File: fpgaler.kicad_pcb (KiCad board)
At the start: 4 copper layers, 245.2 x 139.3 mm, 252 parts, among them J1 USB_C_Receptacle_USB2.0, J2 BATT, J3 JTAG, J4 FTDI_RST, J5 VGA, J6 DB9 Expander, Q1 BC817, SW1 RotaryEncoder_Switch, SW2 RotaryEncoder_Switch, SW3 K1, SW4 K2, SW5 PROGRAMN, SW6 K3, SW7 FPGA GSRN, SW8 K4, U1 TLV62569DRL, U10 XC6206PxxxMR, U11 IS62WV51216BLL-55TLI, U2 TLV62569DRL, U3 NCP115-2.5, U4 BQ24232, U5 93LC56BT-I/OT, U6 FT2232HL, U7 CAT24C128, U8 LFE5U-25F-8MG285C, U9 W25Q128JVP, X1 27MHz, Y1 7M-12.000MAAJ

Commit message: Routing sram
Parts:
- added R126: 22R, Resistor_SMD:R_0402_1005Metric_Pad0.72x0.64mm_HandSolder, F.Cu at (212.6, 117.6)
- added R127: 22R, Resistor_SMD:R_0402_1005Metric_Pad0.72x0.64mm_HandSolder, F.Cu at (208.9, 117.9)
- added R128: 22R, Resistor_SMD:R_0402_1005Metric_Pad0.72x0.64mm_HandSolder, F.Cu at (212.6, 116.6)
- added R129: 22R, Resistor_SMD:R_0402_1005Metric_Pad0.72x0.64mm_HandSolder, F.Cu at (212.6, 115.6)
- added R130: 22R, Resistor_SMD:R_0402_1005Metric_Pad0.72x0.64mm_HandSolder, F.Cu at (212.6, 101.4)
- added R131: 22R, Resistor_SMD:R_0402_1005Metric_Pad0.72x0.64mm_HandSolder, F.Cu at (212.6, 100.4)
- added R132: 22R, Resistor_SMD:R_0402_1005Metric_Pad0.72x0.64mm_HandSolder, F.Cu at (212.6, 102.4)
- added R133: 22R, Resistor_SMD:R_0402_1005Metric_Pad0.72x0.64mm_HandSolder, F.Cu at (212.6, 105.4)
- added R134: 22R, Resistor_SMD:R_0402_1005Metric_Pad0.72x0.64mm_HandSolder, F.Cu at (212.6, 104.4)
- added R135: 22R, Resistor_SMD:R_0402_1005Metric_Pad0.72x0.64mm_HandSolder, F.Cu at (212.6, 103.4)
- added R136: 22R, Resistor_SMD:R_0402_1005Metric_Pad0.72x0.64mm_HandSolder, F.Cu at (208.9, 106.9)
- added R137: 22R, Resistor_SMD:R_0402_1005Metric_Pad0.72x0.64mm_HandSolder, F.Cu at (208.9, 108.9)
- added R138: 22R, Resistor_SMD:R_0402_1005Metric_Pad0.72x0.64mm_HandSolder, F.Cu at (212.6, 106.4)
- added R139: 22R, Resistor_SMD:R_0402_1005Metric_Pad0.72x0.64mm_HandSolder, F.Cu at (212.6, 107.4)
- added R140: 22R, Resistor_SMD:R_0402_1005Metric_Pad0.72x0.64mm_HandSolder, F.Cu at (208.9, 107.9)
- added R141: 22R, Resistor_SMD:R_0402_1005Metric_Pad0.72x0.64mm_HandSolder, F.Cu at (208.9, 110.9)
- added R142: 22R, Resistor_SMD:R_0402_1005Metric_Pad0.72x0.64mm_HandSolder, F.Cu at (208.9, 109.9)
- added R143: 22R, Resistor_SMD:R_0402_1005Metric_Pad0.72x0.64mm_HandSolder, F.Cu at (208.9, 111.9)
- added R144: 22R, Resistor_SMD:R_0402_1005Metric_Pad0.72x0.64mm_HandSolder, F.Cu at (212.6, 109.4)
- added R145: 22R, Resistor_SMD:R_0402_1005Metric_Pad0.72x0.64mm_HandSolder, F.Cu at (212.6, 108.4)
- added R146: 22R, Resistor_SMD:R_0402_1005Metric_Pad0.72x0.64mm_HandSolder, F.Cu at (212.6, 110.5)
- added R147: 22R, Resistor_SMD:R_0402_1005Metric_Pad0.72x0.64mm_HandSolder, F.Cu at (212.6, 112.6)
- added R148: 22R, Resistor_SMD:R_0402_1005Metric_Pad0.72x0.64mm_HandSolder, F.Cu at (208.9, 113.9)
- added R149: 22R, Resistor_SMD:R_0402_1005Metric_Pad0.72x0.64mm_HandSolder, F.Cu at (208.9, 112.9)
- added R150: 22R, Resistor_SMD:R_0402_1005Metric_Pad0.72x0.64mm_HandSolder, F.Cu at (212.6, 111.6)
- added R151: 22R, Resistor_SMD:R_0402_1005Metric_Pad0.72x0.64mm_HandSolder, F.Cu at (212.6, 113.6)
- added R152: 22R, Resistor_SMD:R_0402_1005Metric_Pad0.72x0.64mm_HandSolder, F.Cu at (208.9, 115.9)
- added R153: 22R, Resistor_SMD:R_0402_1005Metric_Pad0.72x0.64mm_HandSolder, F.Cu at (208.9, 114.9)
- added R154: 22R, Resistor_SMD:R_0402_1005Metric_Pad0.72x0.64mm_HandSolder, F.Cu at (208.9, 116.9)
- added R155: 22R, Resistor_SMD:R_0402_1005Metric_Pad0.72x0.64mm_HandSolder, F.Cu at (212.6, 114.6)
- added R156: 22R, Resistor_SMD:R_0402_1005Metric_Pad0.72x0.64mm_HandSolder, F.Cu at (208.9, 102.9)
- added R157: 22R, Resistor_SMD:R_0402_1005Metric_Pad0.72x0.64mm_HandSolder, F.Cu at (208.9, 104.9)
- added R158: 22R, Resistor_SMD:R_0402_1005Metric_Pad0.72x0.64mm_HandSolder, F.Cu at (208.9, 105.9)
- added R159: 22R, Resistor_SMD:R_0402_1005Metric_Pad0.72x0.64mm_HandSolder, F.Cu at (208.9, 101.9)
- added R160: 22R, Resistor_SMD:R_0402_1005Metric_Pad0.72x0.64mm_HandSolder, F.Cu at (208.9, 98.9)
- added R161: 22R, Resistor_SMD:R_0402_1005Metric_Pad0.72x0.64mm_HandSolder, F.Cu at (208.9, 103.9)
- added R162: 22R, Resistor_SMD:R_0402_1005Metric_Pad0.72x0.64mm_HandSolder, F.Cu at (208.9, 99.9)
- added R163: 22R, Resistor_SMD:R_0402_1005Metric_Pad0.72x0.64mm_HandSolder, F.Cu at (208.9, 100.9)
- added R164: 22R, Resistor_SMD:R_0402_1005Metric_Pad0.72x0.64mm_HandSolder, F.Cu at (212.6, 98.4)
- added R165: 22R, Resistor_SMD:R_0402_1005Metric_Pad0.72x0.64mm_HandSolder, F.Cu at (212.6, 99.4)
- R10, R114, R115, R116, R117, R118, R119, R120, R121, R122, R123, R124, R125, R52, R53, R54, R55, R56, R57, R59, R60, R61, R67, R68, R69, R70, R73, R74, R75, R76, R77, R78, R79, R80, R81, R82, R83, R84, R85, R86, R87, R88, R89, R9, R90: footprint Resistor_SMD:R_0603_1608Metric -> Resistor_SMD:R_0402_1005Metric_Pad0.72x0.64mm_HandSolder
- moved C57 34.7 mm to (250.6, 93.5)
- moved C58 34.7 mm to (250.8, 110.3)
- moved TP58 27.5 mm to (237.2, 127.0)
- moved TP59 27.5 mm to (239.7, 125.7)
- moved TP60 27.5 mm to (239.7, 128.2)
- moved TP62 27.5 mm to (239.7, 130.8)
- moved TP64 27.5 mm to (234.6, 130.8)
- moved TP61 27.5 mm to (242.2, 129.5)
- moved TP63 27.5 mm to (237.2, 129.5)
- moved U11 8.55 mm to (225.1, 107.7)
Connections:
- U8 pad A16: unconnected-(U8F-PL20B-PadA16) -> Net-(U8F-PL20B)
- U8 pad A17: /FPGA/A5 -> Net-(U8F-PL23A/PCLKT7_1)
- U8 pad A2: unconnected-(U8C-PR20C/GR_PCLK2_0-PadA2) -> /FPGA/VGA_B0
- U8 pad A3: unconnected-(U8C-PR20A/GR_PCLK2_1-PadA3) -> /FPGA/VGA_G1
- U8 pad B1: unconnected-(U8C-PR23B/PCLKC2_1-PadB1) -> /FPGA/VGA_B2
- U8 pad B15: /FPGA/A7 -> Net-(U8F-PL20A/GR_PCLK7_1)
- U8 pad B17: /FPGA/A6 -> Net-(U8F-PL23B/PCLKC7_1)
- U8 pad B18: /FPGA/A12 -> Net-(U8F-PL23C/PCLKT7_0)
- U8 pad B2: unconnected-(U8C-PR20B-PadB2) -> /FPGA/VGA_G2
- U8 pad B4: unconnected-(U8C-PR14C/VREF1_2-PadB4) -> /FPGA/VGA_R0
- U8 pad C1: unconnected-(U8C-PR23C/PCLKT2_0-PadC1) -> /FPGA/VGA_HSYNC
- U8 pad C15: /FPGA/~{OE} -> Net-(U8F-PL14C/VREF1_7)
- U8 pad C16: /FPGA/~{UB} -> Net-(U8F-PL20C/GR_PCLK7_0)
- U8 pad C17: /FPGA/A13 -> Net-(U8F-PL23D/PCLKC7_0)
- U8 pad C18: /FPGA/A14 -> Net-(U8E-PL26B/PCLKC6_1)
- U8 pad C2: unconnected-(U8C-PR17B-PadC2) -> /FPGA/VGA_G0
- U8 pad C3: unconnected-(U8C-PR14D-PadC3) -> /FPGA/VGA_R1
- U8 pad D1: unconnected-(U8C-PR23D/PCLKC2_0-PadD1) -> /FPGA/VGA_VSYNC
- U8 pad D15: /FPGA/~{LB} -> Net-(U8F-PL17A)
- U8 pad D16: /FPGA/IO15 -> Net-(U8F-PL17B)
- U8 pad D17: /FPGA/A15 -> Net-(U8E-PL26A/PCLKT6_1)
- U8 pad D18: /FPGA/A16 -> Net-(U8E-PL26C/PCLKT6_0)
- U8 pad D2: unconnected-(U8C-PR23A/PCLKT2_1-PadD2) -> /FPGA/VGA_B1
- U8 pad D3: unconnected-(U8C-PR17A-PadD3) -> /FPGA/VGA_R2
- U8 pad F15: /FPGA/IO14 -> Net-(U8E-PL29C/GR_PCLK6_1)
- U8 pad F16: /FPGA/~{WE} -> Net-(U8E-PL29B)
- U8 pad F17: /FPGA/IO07 -> Net-(U8E-PL29A/GR_PCLK6_0)
- U8 pad F18: /FPGA/IO06 -> Net-(U8E-PL26D/PCLKC6_0)
- U8 pad G15: /FPGA/IO13 -> Net-(U8E-PL35A)
- U8 pad G16: /FPGA/IO12 -> Net-(U8E-PL29D)
- U8 pad G18: /FPGA/IO05 -> Net-(U8E-PL32A)
- U8 pad H15: /FPGA/IO10 -> Net-(U8E-PL35B/VREF1_6)
- U8 pad H16: /FPGA/IO11 -> Net-(U8E-PL35C)
- U8 pad H17: /FPGA/IO04 -> Net-(U8E-PL32B)
- U8 pad H18: /FPGA/IO03 -> Net-(U8E-PL38D)
- U8 pad J16: /FPGA/IO09 -> Net-(U8E-PL35D)
- U8 pad J17: /FPGA/IO02 -> Net-(U8E-PL38C)
- U8 pad J18: /FPGA/IO01 -> Net-(U8E-PL41A)
- U8 pad K15: /FPGA/IO08 -> Net-(U8E-PL41D)
- U8 pad K16: /FPGA/A18 -> Net-(U8E-PL41C)
- U8 pad K17: /FPGA/IO00 -> Net-(U8E-PL44A)
- U8 pad K18: /FPGA/~{CS1} -> Net-(U8E-PL41B)
- U8 pad L15: /FPGA/A9 -> Net-(U8E-PL44C)
- U8 pad L16: /FPGA/A8 -> Net-(U8E-PL44D)
- U8 pad L18: /FPGA/A0 -> Net-(U8E-PL44B)
- U8 pad M16: /FPGA/A10 -> Net-(U8E-PL47C/LLC_GPLL0T_IN)
- U8 pad M17: /FPGA/A1 -> Net-(U8E-PL47D/LLC_GPLL0C_IN)
- U8 pad M18: /FPGA/A2 -> Net-(U8G-PB6B/D4/MOSI2/IO4)
- U8 pad N15: /FPGA/A4 -> Net-(U8G-PB4A/D7/IO7)
- U8 pad N16: /FPGA/A11 -> Net-(U8G-PB4B/D6/IO6)
- U8 pad N17: /FPGA/A3 -> Net-(U8G-PB6A/D5/MISO2/IO5)
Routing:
- net Net-(U8G-PB4A/D7/IO7): track 0.00 -> 15.2 mm, vias 0 -> 2
- net Net-(U8G-PB6A/D5/MISO2/IO5): track 0.00 -> 13.8 mm
- net Net-(U8E-PL26A/PCLKT6_1): track 0.00 -> 13.2 mm
- net Net-(U8E-PL29B): track 0.00 -> 12.8 mm
- net Net-(U8F-PL23C/PCLKT7_0): track 0.00 -> 12.8 mm
- net Net-(U8F-PL23D/PCLKC7_0): track 0.00 -> 12.7 mm
- net Net-(U8G-PB6B/D4/MOSI2/IO4): track 0.00 -> 12.3 mm
- net Net-(U8E-PL26C/PCLKT6_0): track 0.00 -> 12.2 mm
- net Net-(U8E-PL47D/LLC_GPLL0C_IN): track 0.00 -> 12.2 mm
- net Net-(U8E-PL29A/GR_PCLK6_0): track 0.00 -> 11.5 mm
- net Net-(U8E-PL26B/PCLKC6_1): track 0.00 -> 11.2 mm
- net /FPGA/A14: track 25.0 -> 35.5 mm, vias 0 -> 1
- net Net-(U8G-PB4B/D6/IO6): track 0.00 -> 10.5 mm, vias 0 -> 2
- net Net-(U8E-PL44B): track 0.00 -> 10.4 mm
- net Net-(U8E-PL47C/LLC_GPLL0T_IN): track 0.00 -> 10.3 mm, vias 0 -> 2
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
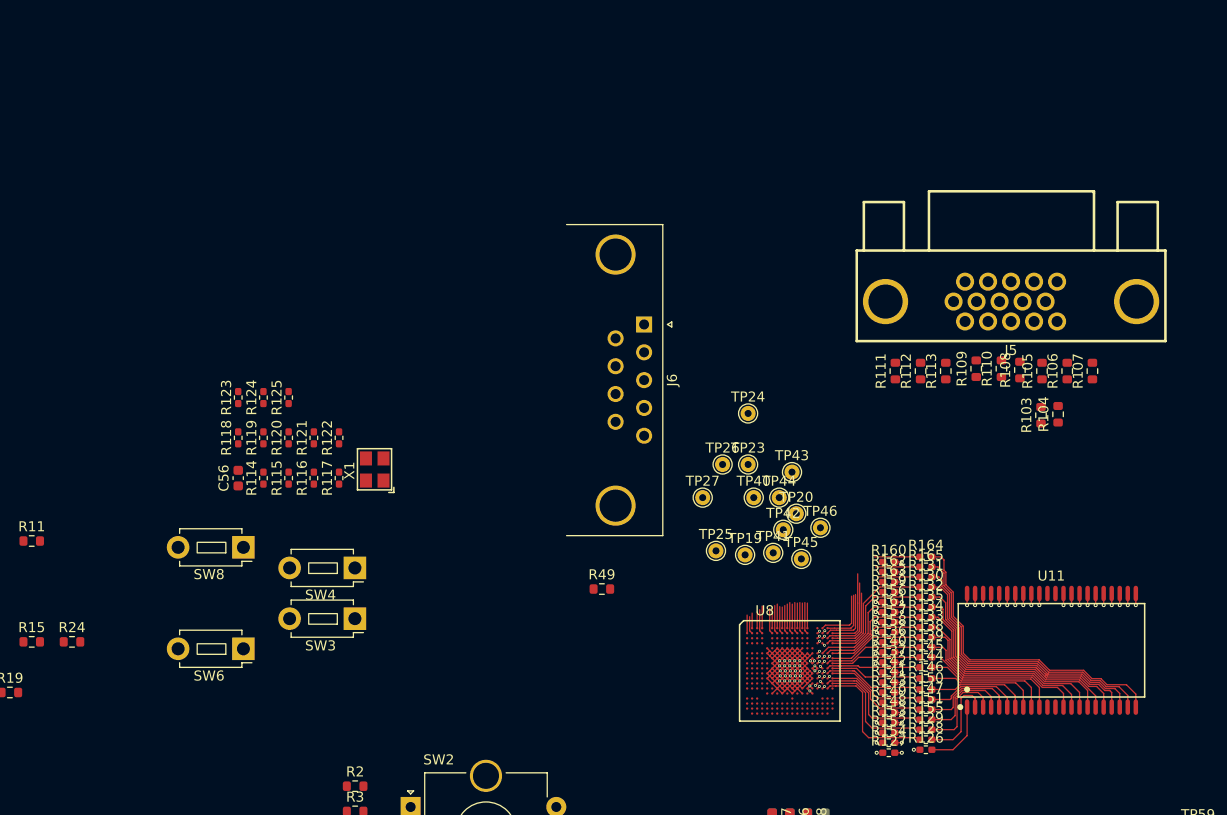
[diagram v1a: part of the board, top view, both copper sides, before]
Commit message: Complete SRAM, and routing VGA
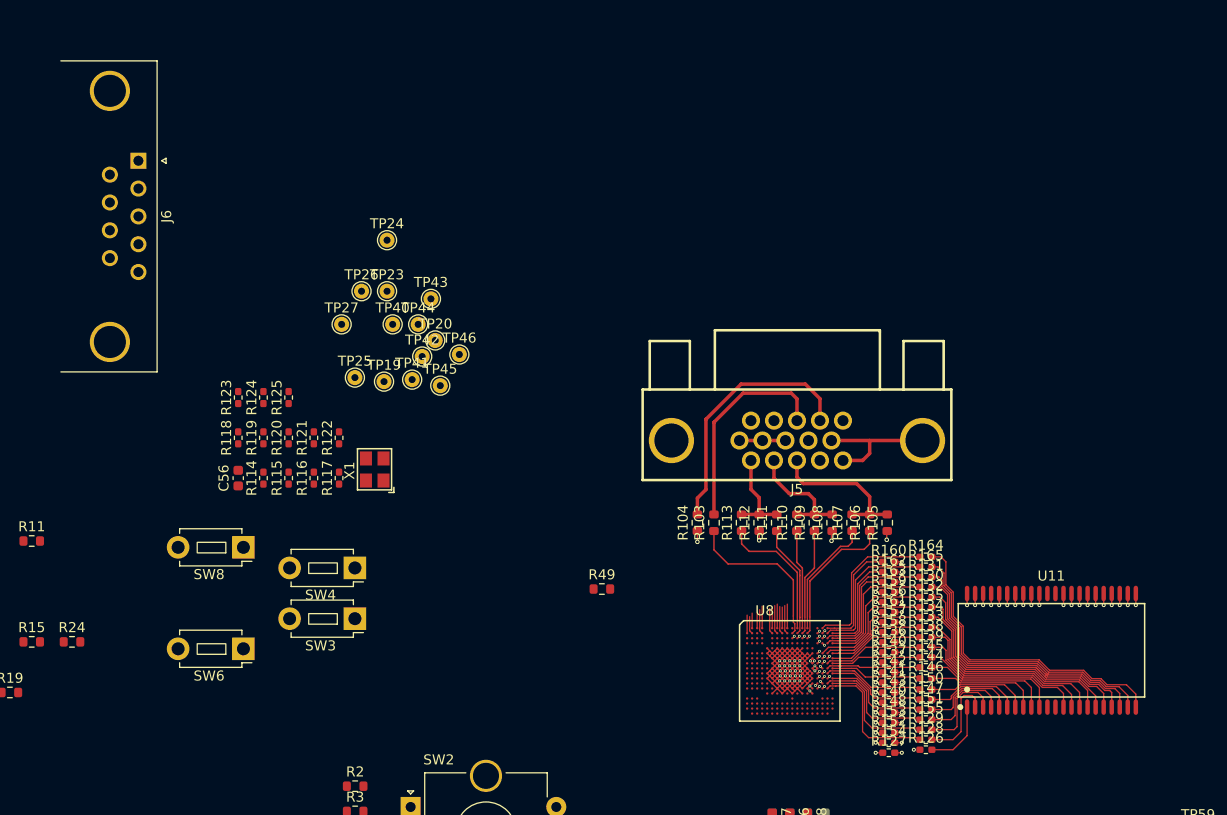
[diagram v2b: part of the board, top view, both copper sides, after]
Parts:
- moved J6 52.9 mm to (134.2, 59.0)
- moved TP23 39.9 mm to (158.9, 72.0)
- moved TP24 39.9 mm to (158.9, 66.9)
- moved TP26 39.9 mm to (156.4, 72.0)
- moved TP40 39.9 mm to (159.5, 75.2)
- moved TP41 39.9 mm to (161.4, 80.8)
- moved TP42 39.9 mm to (162.4, 78.5)
- moved TP43 39.9 mm to (163.3, 72.7)
- moved TP19 39.9 mm to (158.7, 81.0)
- moved TP20 39.9 mm to (163.8, 76.8)
- moved TP25 39.9 mm to (155.8, 80.5)
- moved TP27 39.9 mm to (154.4, 75.2)
- moved TP44 39.9 mm to (162.1, 75.2)
- moved TP45 39.9 mm to (164.2, 81.3)
- moved TP46 39.9 mm to (166.2, 78.2)
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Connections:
- R114 pad 2: Net-(U8A-PT29A/PCLKT0_0) -> Net-(U8B-PT33A/PCLKT1_1)
- R115 pad 2: Net-(U8A-PT29B/PCLKC0_0) -> Net-(U8B-PT33B/PCLKC1_1)
- R131 pad 1: Net-(U8E-PL26B/PCLKC6_1) -> Net-(U8F-PL23D/PCLKC7_0)
- R131 pad 2: /FPGA/A17 -> /FPGA/A14
- R160 pad 1: Net-(U8F-PL20B) -> Net-(U8F-PL23A/PCLKT7_1)
- R160 pad 2: /FPGA/A5 -> /FPGA/A17
- R162 pad 1: Net-(U8F-PL23A/PCLKT7_1) -> Net-(U8F-PL23C/PCLKT7_0)
- R162 pad 2: /FPGA/A6 -> unconnected-(R162-Pad2)
- R163 pad 1: Net-(U8F-PL23B/PCLKC7_1) -> Net-(U8E-PL26B/PCLKC6_1)
- R163 pad 2: /FPGA/A14 -> /FPGA/A6
- R164 pad 1: Net-(U8F-PL23C/PCLKT7_0) -> Net-(U8F-PL20B)
- R165 pad 1: Net-(U8F-PL23D/PCLKC7_0) -> Net-(U8F-PL23B/PCLKC7_1)
- TP19 pad 1: Net-(U8A-PT27A/PCLKT0_1) -> unconnected-(TP19-Pad1)
- TP20 pad 1: Net-(U8A-PT27B/PCLKC0_1) -> unconnected-(TP20-Pad1)
- TP23 pad 1: Net-(U8B-PT33A/PCLKT1_1) -> unconnected-(TP23-Pad1)
- TP24 pad 1: Net-(U8B-PT33B/PCLKC1_1) -> unconnected-(TP24-Pad1)
- TP40 pad 1: Net-(U8F-PL2A) -> unconnected-(TP40-Pad1)
- TP41 pad 1: Net-(U8F-PL2B) -> unconnected-(TP41-Pad1)
- TP42 pad 1: Net-(U8F-PL5A) -> unconnected-(TP42-Pad1)
- TP43 pad 1: Net-(U8F-PL8A) -> unconnected-(TP43-Pad1)
- TP44 pad 1: Net-(U8F-PL8B) -> unconnected-(TP44-Pad1)
- TP45 pad 1: Net-(U8F-PL14A) -> unconnected-(TP45-Pad1)
- TP46 pad 1: Net-(U8F-PL14B) -> unconnected-(TP46-Pad1)
- U8 pad A10: Net-(U8A-PT27B/PCLKC0_1) -> unconnected-(U8A-PT27B/PCLKC0_1-PadA10)
- U8 pad A11: Net-(U8A-PT27A/PCLKT0_1) -> /FPGA/VGA_R2
- U8 pad A12: Net-(U8F-PL5A) -> /FPGA/VGA_G2
- U8 pad A13: Net-(U8F-PL14B) -> /FPGA/VGA_B2
- U8 pad A2: /FPGA/VGA_B0 -> unconnected-(U8C-PR20C/GR_PCLK2_0-PadA2)
- U8 pad A3: /FPGA/VGA_G1 -> unconnected-(U8C-PR20A/GR_PCLK2_1-PadA3)
- U8 pad B1: /FPGA/VGA_B2 -> unconnected-(U8C-PR23B/PCLKC2_1-PadB1)
- U8 pad B10: Net-(U8A-PT29A/PCLKT0_0) -> /FPGA/VGA_HSYNC
- U8 pad B11: /FPGA/sda -> /FPGA/VGA_R0
- U8 pad B12: Net-(U8F-PL2B) -> /FPGA/VGA_G1
- U8 pad B13: Net-(U8F-PL14A) -> /FPGA/VGA_B1
- U8 pad B2: /FPGA/VGA_G2 -> unconnected-(U8C-PR20B-PadB2)
- U8 pad B4: /FPGA/VGA_R0 -> unconnected-(U8C-PR14C/VREF1_2-PadB4)
- U8 pad C1: /FPGA/VGA_HSYNC -> unconnected-(U8C-PR23C/PCLKT2_0-PadC1)
- U8 pad C10: Net-(U8A-PT29B/PCLKC0_0) -> /FPGA/VGA_VSYNC
- U8 pad C11: /FPGA/scl -> /FPGA/VGA_R1
- U8 pad C12: Net-(U8F-PL2A) -> /FPGA/VGA_G0
- U8 pad C13: Net-(U8F-PL8B) -> /FPGA/VGA_B0
- U8 pad C2: /FPGA/VGA_G0 -> unconnected-(U8C-PR17B-PadC2)
- U8 pad C3: /FPGA/VGA_R1 -> unconnected-(U8C-PR14D-PadC3)
- U8 pad D1: /FPGA/VGA_VSYNC -> unconnected-(U8C-PR23D/PCLKC2_0-PadD1)
- U8 pad D13: Net-(U8F-PL8A) -> unconnected-(U8F-PL8A-PadD13)
- U8 pad D2: /FPGA/VGA_B1 -> unconnected-(U8C-PR23A/PCLKT2_1-PadD2)
- U8 pad D3: /FPGA/VGA_R2 -> unconnected-(U8C-PR17A-PadD3)
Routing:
- net GND: track 98.7 -> 128.0 mm
- net /FPGA/A17: track 0.70 -> 26.5 mm, vias 1 -> 2
- net /VSYNC: track 0.00 -> 25.4 mm
- net /HSYNC: track 0.00 -> 21.0 mm
- net /FPGA/VGA_VSYNC: track 0.00 -> 18.6 mm, vias 0 -> 2
- net /FPGA/VGA_HSYNC: track 0.00 -> 16.5 mm
- net /B: track 0.00 -> 15.0 mm
- net /FPGA/VGA_B0: track 1.50 -> 15.8 mm, vias 0 -> 2
- net /FPGA/VGA_B1: track 0.00 -> 14.1 mm
- net /FPGA/VGA_R1: track 0.00 -> 13.8 mm, vias 0 -> 2
- net /FPGA/VGA_R2: track 0.00 -> 13.6 mm
- net /FPGA/VGA_G0: track 0.00 -> 11.9 mm, vias 0 -> 2
- net /G: track 0.00 -> 11.7 mm
- net /FPGA/VGA_B2: track 1.80 -> 12.0 mm
- net Net-(U8F-PL20B): track 5.80 -> 15.6 mm
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
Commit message: Place db9, encoder, btn and leds. Continue routing.
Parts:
- removed R49: 0R, Resistor_SMD:R_0603_1608Metric
- added J7: DB9 Expander, Connector_Dsub:DSUB-9_Pins_Horizontal_P2.77x2.84mm_EdgePinOffset4.94mm_Housed_MountingHolesOffset4.94mm, F.Cu at (90.6, 117.1)
- added R166: 22R, Resistor_SMD:R_0402_1005Metric_Pad0.72x0.64mm_HandSolder, F.Cu at (107.3, 41.9)
- added TP10: TestPoint, TestPoint:TestPoint_THTPad_D1.5mm_Drill0.7mm, F.Cu at (105.0, 115.9)
- added TP11: TestPoint, TestPoint:TestPoint_THTPad_D1.5mm_Drill0.7mm, F.Cu at (104.6, 43.4)
- added TP12: TestPoint, TestPoint:TestPoint_THTPad_D1.5mm_Drill0.7mm, F.Cu at (102.0, 42.1)
- added TP13: TestPoint, TestPoint:TestPoint_THTPad_D1.5mm_Drill0.7mm, F.Cu at (104.6, 40.8)
- added TP14: TestPoint, TestPoint:TestPoint_THTPad_D1.5mm_Drill0.7mm, F.Cu at (102.0, 39.6)
- added TP15: TestPoint, TestPoint:TestPoint_THTPad_D1.5mm_Drill0.7mm, F.Cu at (104.6, 38.3)
- added TP16: TestPoint, TestPoint:TestPoint_THTPad_D1.5mm_Drill0.7mm, F.Cu at (102.0, 37.0)
- added TP17: TestPoint, TestPoint:TestPoint_THTPad_D1.5mm_Drill0.7mm, F.Cu at (104.6, 35.8)
- added TP18: TestPoint, TestPoint:TestPoint_THTPad_D1.5mm_Drill0.7mm, F.Cu at (102.0, 34.5)
- added TP2: TestPoint, TestPoint:TestPoint_THTPad_D1.5mm_Drill0.7mm, F.Cu at (105.0, 126.1)
- added TP21: TestPoint, TestPoint:TestPoint_THTPad_D1.5mm_Drill0.7mm, F.Cu at (104.6, 33.2)
- added TP22: TestPoint, TestPoint:TestPoint_THTPad_D1.5mm_Drill0.7mm, F.Cu at (99.0, 86.0)
- added TP28: TestPoint, TestPoint:TestPoint_THTPad_D1.5mm_Drill0.7mm, F.Cu at (96.5, 84.0)
- added TP29: TestPoint, TestPoint:TestPoint_THTPad_D1.5mm_Drill0.7mm, F.Cu at (99.0, 82.0)
- added TP3: TestPoint, TestPoint:TestPoint_THTPad_D1.5mm_Drill0.7mm, F.Cu at (102.5, 124.8)
- added TP30: TestPoint, TestPoint:TestPoint_THTPad_D1.5mm_Drill0.7mm, F.Cu at (96.5, 80.0)
- added TP31: TestPoint, TestPoint:TestPoint_THTPad_D1.5mm_Drill0.7mm, F.Cu at (99.0, 78.0)
- added TP32: TestPoint, TestPoint:TestPoint_THTPad_D1.5mm_Drill0.7mm, F.Cu at (96.5, 76.0)
- added TP33: TestPoint, TestPoint:TestPoint_THTPad_D1.5mm_Drill0.7mm, F.Cu at (99.0, 74.0)
- added TP34: TestPoint, TestPoint:TestPoint_THTPad_D1.5mm_Drill0.7mm, F.Cu at (96.5, 72.0)
- added TP4: TestPoint, TestPoint:TestPoint_THTPad_D1.5mm_Drill0.7mm, F.Cu at (105.0, 123.5)
- added TP5: TestPoint, TestPoint:TestPoint_THTPad_D1.5mm_Drill0.7mm, F.Cu at (102.5, 122.3)
- added TP6: TestPoint, TestPoint:TestPoint_THTPad_D1.5mm_Drill0.7mm, F.Cu at (105.0, 121.0)
- added TP7: TestPoint, TestPoint:TestPoint_THTPad_D1.5mm_Drill0.7mm, F.Cu at (102.5, 119.7)
- added TP8: TestPoint, TestPoint:TestPoint_THTPad_D1.5mm_Drill0.7mm, F.Cu at (105.0, 118.5)
- added TP9: TestPoint, TestPoint:TestPoint_THTPad_D1.5mm_Drill0.7mm, F.Cu at (102.5, 117.2)
- R91, R92, R93, R94: moved to F.Cu
- moved R17 134.4 mm to (126.2, 95.0), turned to 90 degrees
- moved C7 132.0 mm to (128.8, 90.0), turned to 90 degrees
- moved C5 128.6 mm to (126.3, 89.8), turned to 90 degrees
- moved R22 125.8 mm to (129.6, 95.1), turned to 90 degrees
- moved TP27 123.9 mm to (268.5, 123.6), turned to 180 degrees
- moved TP24 123.6 mm to (264.0, 132.0), turned to 180 degrees
- moved TP26 123.1 mm to (266.5, 126.9), turned to 180 degrees
- moved TP23 118.6 mm to (264.0, 126.9), turned to 180 degrees
- moved SW7 118.4 mm to (134.5, 122.8)
- moved SW5 118.4 mm to (124.4, 122.8)
- moved TP25 117.7 mm to (267.2, 118.3), turned to 180 degrees
- moved TP40 114.6 mm to (263.4, 123.6), turned to 180 degrees
- moved C58 112.3 mm to (146.9, 67.5)
- moved TP19 111.9 mm to (264.3, 117.9), turned to 180 degrees
- moved TP43 110.1 mm to (259.6, 126.2), turned to 180 degrees
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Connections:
- C24 pad 1: Net-(U6-OSCO) -> /FPGA/REF_CLK
- J6 pad 1: /FPGA/DB1 -> /P1_DB1
- J6 pad 2: /FPGA/DB3 -> /P1_DB3
- J6 pad 3: /FPGA/DB2 -> /P1_DB2
- J6 pad 4: /FPGA/DB4 -> /P1_DB4
- J6 pad 5: /FPGA/DB5 -> /P1_DB5
- J6 pad 6: /FPGA/DB6 -> /P1_DB6
- J6 pad 7: /FPGA/DB7 -> /P1_DB7
- J6 pad 8: /FPGA/DB8 -> /P1_DB8
- J6 pad 9: /FPGA/DB9 -> /P1_DB9
- R117 pad 2: /FPGA/DB1 -> /P0_DB1
- R118 pad 1: Net-(U8D-PR26B/PCLKC3_1) -> Net-(U8D-PR44B)
- R118 pad 2: /FPGA/DB2 -> /P0_DB2
- R119 pad 2: /FPGA/DB3 -> /P0_DB3
- R120 pad 1: Net-(U8D-PR26D/PCLKC3_0) -> Net-(U8D-PR44C)
- R120 pad 2: /FPGA/DB4 -> /P0_DB4
- R121 pad 1: Net-(U8D-PR29A/GR_PCLK3_0) -> Net-(U8D-PR44D)
- R121 pad 2: /FPGA/DB5 -> /P0_DB5
- R122 pad 2: /FPGA/DB6 -> /P0_DB6
- R123 pad 2: /FPGA/DB7 -> /P0_DB7
- R124 pad 1: Net-(U8D-PR29D) -> Net-(U8D-PR47C/LRC_GPLL0T_IN)
- R124 pad 2: /FPGA/DB8 -> /P0_DB8
- R125 pad 1: Net-(U8D-PR32A) -> Net-(U8D-PR47D/LRC_GPLL0C_IN)
- R125 pad 2: /FPGA/DB9 -> /P0_DB9
- R162 pad 2: unconnected-(R162-Pad2) -> /FPGA/A5
- R73 pad 1: Net-(U8D-PR35A) -> Net-(U8C-PR2A)
- R73 pad 2: /L7 -> /P1_DB1
- R74 pad 1: Net-(U8D-PR35B/VREF1_3) -> Net-(U8C-PR2B/S0_IN)
- R74 pad 2: /L6 -> /P1_DB2
- R75 pad 1: Net-(U8D-PR35C) -> Net-(U8C-PR5A)
- R75 pad 2: /L5 -> /P1_DB3
- R76 pad 1: Net-(U8D-PR35D) -> Net-(U8C-PR5B)
- R76 pad 2: /L4 -> /P1_DB4
- R77 pad 1: Net-(U8D-PR38A) -> Net-(U8C-PR8A)
- R77 pad 2: /L3 -> /P1_DB5
- R78 pad 1: Net-(U8D-PR38B) -> Net-(U8C-PR8B)
- R78 pad 2: /L2 -> /P1_DB6
- R79 pad 1: Net-(U8D-PR38C) -> Net-(U8C-PR11A)
- R79 pad 2: /L1 -> /P1_DB7
- R80 pad 1: Net-(U8D-PR38D) -> Net-(U8C-PR11B)
- R80 pad 2: /L0 -> /P1_DB8
- R86 pad 1: Net-(U8D-PR44B) -> unconnected-(R86-Pad1)
- R87 pad 1: Net-(U8D-PR44C) -> unconnected-(R87-Pad1)
- R88 pad 1: Net-(U8D-PR44D) -> unconnected-(R88-Pad1)
- R89 pad 1: Net-(U8D-PR47C/LRC_GPLL0T_IN) -> unconnected-(R89-Pad1)
- R90 pad 1: Net-(U8D-PR47D/LRC_GPLL0C_IN) -> unconnected-(R90-Pad1)
- U6 pad 3: Net-(U6-OSCO) -> /FPGA/REF_CLK
- U8 pad A11: /FPGA/VGA_R2 -> /FPGA/VGA_R1
- U8 pad A4: unconnected-(U8C-PR11B-PadA4) -> Net-(U8C-PR11B)
- U8 pad A6: unconnected-(U8C-PR11A-PadA6) -> Net-(U8C-PR11A)
- U8 pad A7: unconnected-(U8C-PR8B-PadA7) -> Net-(U8C-PR8B)
- U8 pad B6: unconnected-(U8C-PR8A-PadB6) -> Net-(U8C-PR8A)
- U8 pad B7: unconnected-(U8C-PR2B/S0_IN-PadB7) -> Net-(U8C-PR2B/S0_IN)
- U8 pad C11: /FPGA/VGA_R1 -> /FPGA/VGA_R2
- U8 pad C6: unconnected-(U8C-PR5B-PadC6) -> Net-(U8C-PR5B)
- U8 pad C7: unconnected-(U8C-PR2A-PadC7) -> Net-(U8C-PR2A)
- U8 pad D4: unconnected-(U8C-PR14A-PadD4) -> Net-(U8C-PR14A)
- U8 pad D6: unconnected-(U8C-PR5A-PadD6) -> Net-(U8C-PR5A)
- U8 pad F1: Net-(U8D-PR35C) -> /L5
- U8 pad F2: Net-(U8D-PR32A) -> unconnected-(U8D-PR32A-PadF2)
- U8 pad F3: Net-(U8D-PR26D/PCLKC3_0) -> unconnected-(U8D-PR26D/PCLKC3_0-PadF3)
- U8 pad G4: Net-(U8D-PR26B/PCLKC3_1) -> unconnected-(U8D-PR26B/PCLKC3_1-PadG4)
- U8 pad H1: Net-(U8D-PR35D) -> /L4
- U8 pad H2: Net-(U8D-PR29D) -> unconnected-(U8D-PR29D-PadH2)
- U8 pad H3: Net-(U8D-PR29A/GR_PCLK3_0) -> /L0
- U8 pad J1: Net-(U8D-PR35B/VREF1_3) -> /L6
- U8 pad J2: Net-(U8D-PR35A) -> /L7
- U8 pad K4: Net-(U8D-PR38A) -> /L3
- U8 pad L4: Net-(U8D-PR38B) -> /L2
- U8 pad N3: Net-(U8D-PR38D) -> unconnected-(U8D-PR38D-PadN3)
- U8 pad N4: Net-(U8D-PR38C) -> /L1
- Y1 pad 3: Net-(U6-OSCO) -> /FPGA/REF_CLK
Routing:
- net Net-(U8D-PR44D): track 0.00 -> 49.4 mm
- net Net-(U8D-PR47D/LRC_GPLL0C_IN): track 0.00 -> 47.4 mm
- net Net-(U8D-PR44C): track 0.00 -> 47.3 mm
- net Net-(U8D-PR47C/LRC_GPLL0T_IN): track 0.00 -> 45.9 mm
- net Net-(U8D-PR44B): track 0.00 -> 44.9 mm
- net /K4: track 0.00 -> 44.1 mm
- net /K1: track 0.00 -> 43.4 mm
- net Net-(U8C-PR8B): track 0.00 -> 40.5 mm
- net /K3: track 0.00 -> 39.3 mm
- net Net-(U8C-PR2A): track 0.00 -> 39.0 mm
- net /K2: track 0.00 -> 38.1 mm
- net Net-(U8C-PR11A): track 0.00 -> 37.6 mm
- net Net-(U8C-PR2B/S0_IN): track 0.00 -> 37.1 mm
- net Net-(U8C-PR5A): track 0.00 -> 36.8 mm
- net Net-(U8C-PR11B): track 0.00 -> 35.2 mm
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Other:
- board size 245.2 x 139.3 mm -> 188 x 165.2 mm
